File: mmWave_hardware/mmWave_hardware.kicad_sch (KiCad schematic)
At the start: 32 parts, among them U1 IWRL6432BDBAAMFR, U2 W25Q128JVS, U3 AMS1117-3.3, Y1 40.000

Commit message: sch
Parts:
- added C18, C19: 10u, symbol Device:C_Small
- added J1: Conn_02x08_Top_Bottom, symbol Connector_Generic:Conn_02x08_Top_Bottom
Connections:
- net 3v3: now also U3.2 (VO), C19.1
- net GND: now also U3.1 (GND), C18.2, C19.2, J1.1 (Pin_1)
- net NRST_MAIN: now also J1.15 (Pin_15)
- net RS232_RX: now also J1.14 (Pin_14)
- net RS232_TX: now also J1.13 (Pin_13)
- net SPI0_CLK: now also J1.9 (Pin_9)
- net SPI0_CS0_N: now also J1.10 (Pin_10)
- net SPI0_MISO: now also J1.11 (Pin_11)
- net SPI0_MOSI: now also J1.12 (Pin_12)
- net TCK: now also J1.2 (Pin_2)
- net TDI: now also J1.4 (Pin_4)
- net TDO: now also J1.5 (Pin_5)
- net TMS: now also J1.3 (Pin_3)
- net UART_RTS: now also J1.6 (Pin_6)
- net UART_RX: now also J1.7 (Pin_7)
- net UART_TX: now also J1.8 (Pin_8)
- net VIN: now reaches U3.3 (VI)
- net VIN: now also C18.1, J1.16 (Pin_16)

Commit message: sch+pcb
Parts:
- added C20: 10u, Capacitor_SMD:C_0603_1608Metric, symbol Device:C_Small
- added C21: 2u2, Capacitor_SMD:C_0603_1608Metric, symbol Device:C_Small
- added U4: TPS5430DDA, Package_SO:TI_SO-PowerPAD-8_ThermalVias, symbol Regulator_Switching:TPS5430DDA
- C1, C15, C2: footprint (none) -> Capacitor_SMD:C_0402_1005Metric_Pad0.74x0.62mm_HandSolder
- C10, C11, C12, C13, C14, C16, C17, C3, C4, C5, C6, C7, C8, C9: footprint (none) -> Capacitor_SMD:C_0603_1608Metric_Pad1.08x0.95mm_HandSolder
- C18, C19: footprint (none) -> Capacitor_SMD:C_0603_1608Metric
- J1: footprint (none) -> Connector_PinHeader_2.54mm:PinHeader_2x08_P2.54mm_Vertical
- R1, R2, R3: footprint (none) -> Resistor_SMD:R_0402_1005Metric
- R4, R5, R6: value 100k -> 10k; footprint (none) -> Resistor_SMD:R_0402_1005Metric
- TP1, TP2, TP3, TP4, TP5: footprint (none) -> TestPoint:TestPoint_Pad_D2.0mm
- Y1: footprint (none) -> Crystal:Crystal_SMD_3225-4Pin_3.2x2.5mm_HandSoldering
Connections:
- net GND: now also C13.2, C14.2, C20.2, C21.2, U4.6 (GND), U4.9 (GNDPAD)
- net VIN: now also C20.1, C21.1, U4.5 (EN), U4.7 (VIN)
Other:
- moved on the sheet: C18, C19, U3

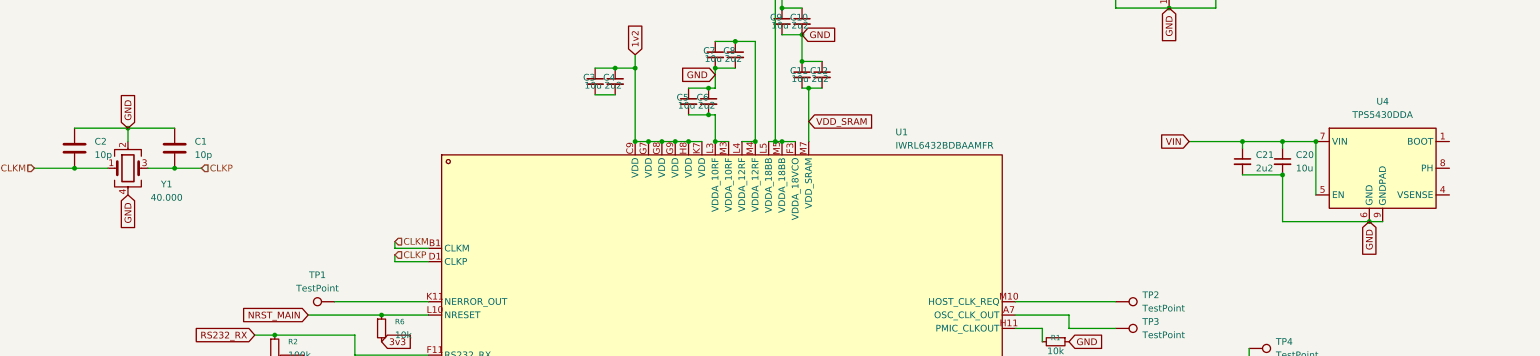
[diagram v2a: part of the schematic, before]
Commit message: new buck conv
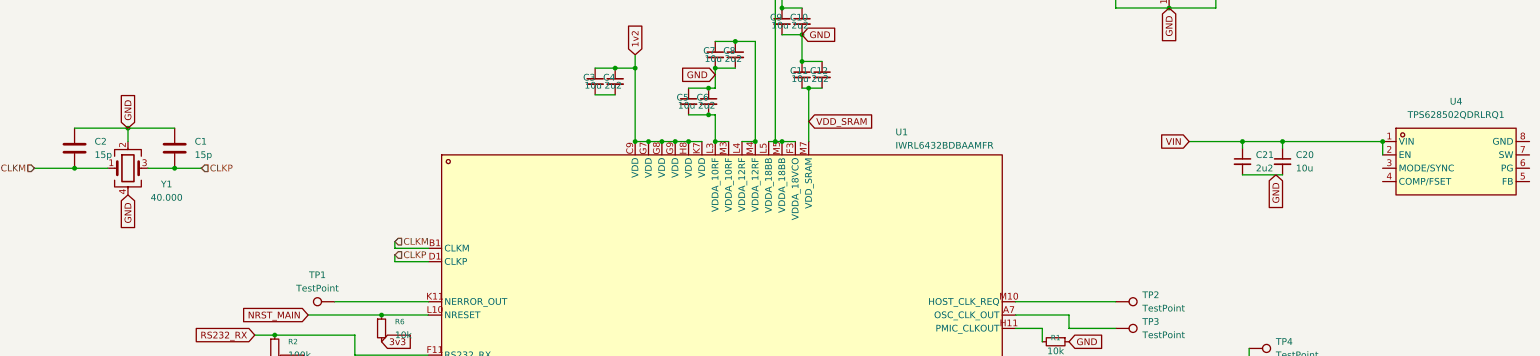
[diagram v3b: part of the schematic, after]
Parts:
- removed U4: TPS5430DDA, Package_SO:TI_SO-PowerPAD-8_ThermalVias, symbol Regulator_Switching:TPS5430DDA
- added U4: TPS628502QDRLRQ1, easyeda2kicad:SOT-583-8_L2.1-W1.2-P0.50-LS1.6-BR, symbol easyeda2kicad:TPS628502QDRLRQ1
- C1, C2: value 10p -> 15p
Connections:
- net VIN: now also U4.1 (VIN), U4.2 (EN)
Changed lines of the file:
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@@
 	)
 	(junction
-		(at 313.69 62.23)
-		(diameter 0)
-		(color 0 0 0 0)
-	)
-	(junction
 		(at 247.65 204.47)
 		(diameter 0)
@@
 	)
 	(junction
+		(at 326.39 62.23)
+		(diameter 0)
+		(color 0 0 0 0)
+	)
+	(junction
 		(at 269.24 168.91)
 		(diameter 0)
@@
 	)
 	(junction
-		(at 323.85 77.47)
-		(diameter 0)
-		(color 0 0 0 0)
-	)
-	(junction
 		(at 96.52 67.31)
 		(diameter 0)
@@
 	)
 	(junction
-		(at 307.34 68.58)
-		(diameter 0)
-		(color 0 0 0 0)
-	)
-	(junction
 		(at 212.09 62.23)
 		(diameter 0)
@@
 	(wire
 		(pts
+			(xy 326.39 62.23) (xy 326.39 64.77)
+		)
+		(stroke
+			(width 0)
+			(type default)
+		)
+	)
+	(wire
+		(pts
 			(xy 207.01 43.18) (xy 207.01 62.23)
 		)
@@
 	(wire
 		(pts
-			(xy 323.85 77.47) (xy 326.39 77.47)
-		)
-		(stroke
-			(width 0)
-			(type default)
-		)
-	)
-	(wire
-		(pts
 			(xy 293.37 29.21) (xy 294.64 29.21)
 		)
@@
 	(wire
 		(pts
-			(xy 313.69 62.23) (xy 313.69 72.39)
-		)
-		(stroke
-			(width 0)
-			(type default)
-		)
-	)
-	(wire
-		(pts
 			(xy 144.78 179.07) (xy 125.73 179.07)
 		)
@@
 	(wire
 		(pts
-			(xy 307.34 62.23) (xy 313.69 62.23)
+			(xy 307.34 62.23) (xy 326.39 62.23)
 		)
 		(stroke
@@
 	(wire
 		(pts
-			(xy 307.34 68.58) (xy 307.34 77.47)
-		)
-		(stroke
-			(width 0)
-			(type default)
-		)
-	)
-	(wire
-		(pts
 			(xy 199.39 57.15) (xy 199.39 62.23)
 		)
@@
 	(wire
 		(pts
-			(xy 307.34 77.47) (xy 323.85 77.47)
-		)
-		(stroke
-			(width 0)
-			(type default)
-		)
-	)
-	(wire
-		(pts
 			(xy 300.99 107.95) (xy 300.99 106.68)
 		)
@@
 	(global_label "GND"
 		(shape input)
-		(at 323.85 77.47 270)
+		(at 306.07 68.58 270)
 		(fields_autoplaced yes)
 		(effects
@@
 		)
 		(property "Intersheetrefs" "${INTERSHEET_REFS}"
-			(at 323.85 84.3257 90)
+			(at 306.07 75.4357 90)
 			(effects
 				(font
@@
 	)
 	(symbol
-		(lib_id "Regulator_Switching:TPS5430DDA")
-		(at 326.39 67.31 0)
-		(unit 1)
-		(exclude_from_sim no)
-		(in_bom yes)
-		(on_board yes)
-		(dnp no)
-		(fields_autoplaced yes)
-		(property "Reference" "U4"
-			(at 326.39 54.61 0)
-			(effects
-				(font
-					(size 1.27 1.27)
-				)
-			)
-		)
-		(property "Value" "TPS5430DDA"
-			(at 326.39 57.15 0)
-			(effects
-				(font
-					(size 1.27 1.27)
-				)
-			)
-		)
-		(property "Footprint" "Package_SO:TI_SO-PowerPAD-8_ThermalVias"
-			(at 327.66 76.2 0)
-			(effects
-				(font
-					(size 1.27 1.27)
-					(italic yes)
-				)
-				(justify left)
-				(hide yes)
-			)
-		)
-		(property "Datasheet" "http://www.ti.com/lit/ds/symlink/tps5430.pdf"
-			(at 326.39 67.31 0)
-			(effects
-				(font
-					(size 1.27 1.27)
-				)
-				(hide yes)
-			)
-		)
-		(property "Description" "3A, Step Down Swift Converter, Adjustable Output Voltage, 5.5-36V Input Voltage, PowerSO-8"
-			(at 326.39 67.31 0)
-			(effects
-				(font
-					(size 1.27 1.27)
-				)
-				(hide yes)
-			)
-		)
-		(pin "8"
-		)
-		(pin "2"
-		)
-		(pin "1"
-		)
-		(pin "9"
-		)
-		(pin "3"
-		)
-		(pin "7"
-		)
-		(pin "5"
-		)
-		(pin "4"
-		)
-		(pin "6"
-		)
-		(instances
-			(project ""
-				(path "/6162916a-a208-4f68-9876-78e56ce61083"
-					(reference "U4")
-					(unit 1)
-				)
-			)
-		)
-	)
-	(symbol
 		(lib_id "Device:C_Small")
 		(at 215.9 49.53 0)
@@
 	)
 	(symbol
+		(lib_id "easyeda2kicad:TPS628502QDRLRQ1")
+		(at 340.36 66.04 0)
+		(unit 1)
+		(exclude_from_sim no)
+		(in_bom yes)
+		(on_board yes)
+		(dnp no)
+		(fields_autoplaced yes)
+		(property "Reference" "U4"
+			(at 340.36 54.61 0)
+			(effects
+				(font
+					(size 1.27 1.27)
+				)
+			)
+		)
+		(property "Value" "TPS628502QDRLRQ1"
+			(at 340.36 57.15 0)
+			(effects
+				(font
+					(size 1.27 1.27)
+				)
+			)
+		)
+		(property "Footprint" "easyeda2kicad:SOT-583-8_L2.1-W1.2-P0.50-LS1.6-BR"
+			(at 340.36 77.47 0)
+			(effects
+				(font
+					(size 1.27 1.27)
+				)
+				(hide yes)
+			)
+		)
+		(property "Datasheet" ""
+			(at 340.36 66.04 0)
+			(effects
+				(font
+					(size 1.27 1.27)
+				)
+				(hide yes)
+			)
+		)
+		(property "Description" ""
+			(at 340.36 66.04 0)
+			(effects
+				(font
+					(size 1.27 1.27)
+				)
+				(hide yes)
+			)
+		)
+		(property "LCSC Part" "C3193229"
+			(at 340.36 80.01 0)
+			(effects
+				(font
+					(size 1.27 1.27)
+				)
+				(hide yes)
+			)
+		)
+		(pin "4"
+		)
+		(pin "2"
+		)
+		(pin "3"
+		)
+		(pin "5"
+		)
+		(pin "6"
+		)
+		(pin "1"
+		)
+		(pin "8"
+		)
+		(pin "7"
+		)
+		(instances
+			(project ""
+				(path "/6162916a-a208-4f68-9876-78e56ce61083"
+					(reference "U4")
+					(unit 1)
+				)
+			)
+		)
+	)
+	(symbol
 		(lib_id "Device:C_Small")
 		(at 212.09 39.37 0)
@@
 			)
 		)
-		(property "Value" "10p"
+		(property "Value" "15p"
 			(at 81.28 64.7699 0)
 			(effects
@@
 			)
 		)
-		(property "Value" "10p"
+		(property "Value" "15p"
 			(at 100.33 64.7699 0)
 			(effects

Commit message: sch
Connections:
- net QSPI_1: now also U1.B8 (QSPI[1])
- net QSPI_2: no longer U1.B8 (QSPI[1])
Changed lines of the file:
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@@
 		)
 	)
-	(hierarchical_label "QSPI_2"
+	(hierarchical_label "QSPI_1"
 		(shape input)
 		(at 256.54 138.43 0)

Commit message: sch+pcb
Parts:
- added C22, C23, C24, C25: 10u, Capacitor_SMD:C_0603_1608Metric_Pad1.08x0.95mm_HandSolder, symbol Device:C_Small
- added L1: 470n, symbol Device:L
- added L2: 100n, symbol Device:L
- added R7: 100k, Resistor_SMD:R_0402_1005Metric, symbol Device:R_Small
- added R8: 18k, Resistor_SMD:R_0402_1005Metric, symbol Device:R_Small
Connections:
- net 1v8: now also C23.1, C25.1, L2.2
- net GND: now also U4.8 (GND), C22.2, C23.2, C24.2, C25.2, R8.2
- net VIN: now also R7.1
- net at U4.3 (MODE/SYNC): now also R7.2
- net at U4.4 (COMP/FSET): now also R8.1
- net at U4.5 (FB): now also C22.1, C24.1, L1.2, L2.1
- net at U4.7 (SW): now also L1.1
- no-connect marks 1 -> 2

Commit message: sch+pcb
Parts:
- L1, L2: footprint (none) -> Inductor_SMD:L_0805_2012Metric_Pad1.05x1.20mm_HandSolder
- TP1, TP2, TP3, TP4, TP5: footprint TestPoint:TestPoint_Pad_D2.0mm -> TestPoint:TestPoint_Pad_D1.5mm
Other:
- moved on the sheet: C20, C21
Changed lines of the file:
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@@
 	)
 	(junction
+		(at 309.88 62.23)
+		(diameter 0)
+		(color 0 0 0 0)
+	)
+	(junction
 		(at 212.09 204.47)
 		(diameter 0)
@@
 	)
 	(junction
-		(at 299.72 62.23)
-		(diameter 0)
-		(color 0 0 0 0)
-	)
-	(junction
 		(at 256.54 166.37)
 		(diameter 0)
@@
 	)
 	(junction
-		(at 307.34 62.23)
-		(diameter 0)
-		(color 0 0 0 0)
-	)
-	(junction
 		(at 199.39 204.47)
 		(diameter 0)
@@
 	)
 	(junction
+		(at 313.69 62.23)
+		(diameter 0)
+		(color 0 0 0 0)
+	)
+	(junction
 		(at 214.63 204.47)
 		(diameter 0)
@@
 	(wire
 		(pts
-			(xy 299.72 62.23) (xy 307.34 62.23)
-		)
-		(stroke
-			(width 0)
-			(type default)
-		)
-	)
-	(wire
-		(pts
 			(xy 368.3 69.85) (xy 372.11 69.85)
 		)
@@
 	(wire
 		(pts
-			(xy 289.56 62.23) (xy 299.72 62.23)
+			(xy 307.34 62.23) (xy 309.88 62.23)
 		)
 		(stroke
@@
 	(wire
 		(pts
-			(xy 307.34 62.23) (xy 307.34 63.5)
+			(xy 313.69 62.23) (xy 313.69 63.5)
 		)
 		(stroke
@@
 	(wire
 		(pts
+			(xy 313.69 62.23) (xy 317.5 62.23)
+		)
+		(stroke
+			(width 0)
+			(type default)
+		)
+	)
+	(wire
+		(pts
 			(xy 87.63 59.69) (xy 96.52 59.69)
 		)
@@
 	(wire
 		(pts
-			(xy 307.34 62.23) (xy 317.5 62.23)
-		)
-		(stroke
-			(width 0)
-			(type default)
-		)
-	)
-	(wire
-		(pts
 			(xy 176.53 53.34) (xy 180.34 53.34)
 		)
@@
 	(wire
 		(pts
-			(xy 299.72 68.58) (xy 307.34 68.58)
+			(xy 309.88 68.58) (xy 313.69 68.58)
 		)
 		(stroke
@@
 	(wire
 		(pts
+			(xy 313.69 62.23) (xy 309.88 62.23)
+		)
+		(stroke
+			(width 0)
+			(type default)
+		)
+	)
+	(wire
+		(pts
 			(xy 210.82 62.23) (xy 212.09 62.23)
 		)
@@
 	(wire
 		(pts
-			(xy 299.72 62.23) (xy 299.72 63.5)
+			(xy 309.88 62.23) (xy 309.88 63.5)
 		)
 		(stroke
@@
 	(global_label "GND"
 		(shape input)
-		(at 306.07 68.58 270)
+		(at 312.42 68.58 270)
 		(fields_autoplaced yes)
 		(effects
@@
 		)
 		(property "Intersheetrefs" "${INTERSHEET_REFS}"
-			(at 306.07 75.4357 90)
+			(at 312.42 75.4357 90)
 			(effects
 				(font
@@
 	(global_label "VIN"
 		(shape input)
-		(at 289.56 62.23 180)
+		(at 307.34 62.23 180)
 		(fields_autoplaced yes)
 		(effects
@@
 		)
 		(property "Intersheetrefs" "${INTERSHEET_REFS}"
-			(at 283.5509 62.23 0)
+			(at 301.3309 62.23 0)
 			(effects
 				(font
@@
 	(symbol
 		(lib_id "Device:C_Small")
-		(at 307.34 66.04 0)
+		(at 313.69 66.04 0)
 		(unit 1)
 		(exclude_from_sim no)
@@
 		(on_board yes)
 		(dnp no)
-		(fields_autoplaced yes)
 		(property "Reference" "C20"
-			(at 309.88 64.7762 0)
+			(at 311.912 64.77 0)
 			(effects
 				(font
@@
 		)
 		(property "Value" "10u"
-			(at 309.88 67.3162 0)
+			(at 311.912 67.31 0)
 			(effects
 				(font
@@
 		)
 		(property "Footprint" "Capacitor_SMD:C_0603_1608Metric"
-			(at 307.34 66.04 0)
+			(at 313.69 66.04 0)
 			(effects
 				(font
@@
 		)
 		(property "Datasheet" "~"
-			(at 307.34 66.04 0)
+			(at 313.69 66.04 0)
 			(effects
 				(font
@@
 		)
 		(property "Description" "Unpolarized capacitor, small symbol"
-			(at 307.34 66.04 0)
+			(at 313.69 66.04 0)
 			(effects
 				(font
@@
 			)
 		)
-		(property "Footprint" ""
+		(property "Footprint" "Inductor_SMD:L_0805_2012Metric_Pad1.05x1.20mm_HandSolder"
 			(at 375.92 64.77 0)
 			(effects
@@
 			)
 		)
-		(property "Footprint" "TestPoint:TestPoint_Pad_D2.0mm"
+		(property "Footprint" "TestPoint:TestPoint_Pad_D1.5mm"
 			(at 300.99 106.68 0)
 			(effects
@@
 			)
 		)
-		(property "Footprint" "TestPoint:TestPoint_Pad_D2.0mm"
+		(property "Footprint" "TestPoint:TestPoint_Pad_D1.5mm"
 			(at 300.99 111.76 0)
 			(effects
@@
 			)
 		)
-		(property "Footprint" ""
+		(property "Footprint" "Inductor_SMD:L_0805_2012Metric_Pad1.05x1.20mm_HandSolder"
 			(at 359.41 64.77 0)
 			(effects
@@
 			)
 		)
-		(property "Footprint" "TestPoint:TestPoint_Pad_D2.0mm"
+		(property "Footprint" "TestPoint:TestPoint_Pad_D1.5mm"
 			(at 275.59 97.79 0)
 			(effects
@@
 			)
 		)
-		(property "Footprint" "TestPoint:TestPoint_Pad_D2.0mm"
+		(property "Footprint" "TestPoint:TestPoint_Pad_D1.5mm"
 			(at 127 87.63 0)
 			(effects
@@
 			)
 		)
-		(property "Footprint" "TestPoint:TestPoint_Pad_D2.0mm"
+		(property "Footprint" "TestPoint:TestPoint_Pad_D1.5mm"
 			(at 275.59 102.87 0)
 			(effects
@@
 	(symbol
 		(lib_id "Device:C_Small")
-		(at 299.72 66.04 0)
+		(at 309.88 66.04 0)
 		(unit 1)
 		(exclude_from_sim no)
@@
 		(on_board yes)
 		(dnp no)
-		(fields_autoplaced yes)
 		(property "Reference" "C21"
-			(at 302.26 64.7762 0)
+			(at 308.102 64.77 0)
 			(effects
 				(font
@@
 		)
 		(property "Value" "2u2"
-			(at 302.26 67.3162 0)
+			(at 308.102 67.31 0)
 			(effects
 				(font
@@
 		)
 		(property "Footprint" "Capacitor_SMD:C_0603_1608Metric"
-			(at 299.72 66.04 0)
+			(at 309.88 66.04 0)
 			(effects
 				(font
@@
 		)
 		(property "Datasheet" "~"
-			(at 299.72 66.04 0)
+			(at 309.88 66.04 0)
 			(effects
 				(font
@@
 		)
 		(property "Description" "Unpolarized capacitor, small symbol"
-			(at 299.72 66.04 0)
+			(at 309.88 66.04 0)
 			(effects
 				(font

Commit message: antennaaaaaaaaaaaaaaaaaaaaa
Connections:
- net GND: now also C3.2, C4.2
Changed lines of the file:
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@@
+		)
+	)
+	(global_label "GND"
+		(shape input)
+		(at 176.53 53.34 180)
+		(fields_autoplaced yes)
+		(effects
+			(font
+				(size 1.27 1.27)
+			)
+			(justify right)
+		)
+		(property "Intersheetrefs" "${INTERSHEET_REFS}"
+			(at 169.6743 53.34 0)
+			(effects
+				(font
+					(size 1.27 1.27)
+				)
+				(justify right)
+				(hide yes)
+			)
 		)
 	)

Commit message: antennaaaaaaaaaaaaaaaaaaaaa
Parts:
- added AE1, AE2, AE3, AE4, AE5: Antenna, antennas:60GHz_microstrip_inset_patch, symbol Device:Antenna
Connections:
- net RX1: no longer names the net of U1.K1 (RX1)
- net RX1: now also AE5.1 (A)
- net RX2: no longer names the net of U1.H1 (RX2)
- net RX2: now also AE4.1 (A)
- net RX3: no longer names the net of U1.F1 (RX3)
- net RX3: now also AE3.1 (A)
- net TX1: no longer names the net of U1.A3 (TX1)
- net TX1: now also AE2.1 (A)
- net TX2: no longer names the net of U1.A5 (TX2)
- net TX2: now also AE1.1 (A)
